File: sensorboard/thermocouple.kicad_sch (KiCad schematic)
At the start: 8 parts, among them U4 MAX31856

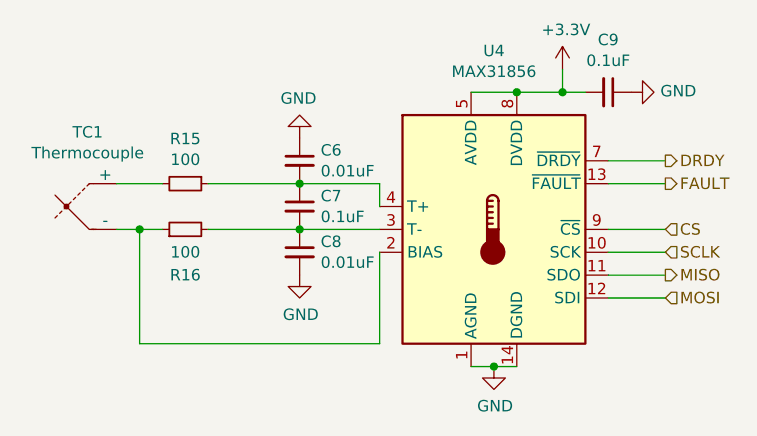
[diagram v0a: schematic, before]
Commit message: updated boost converter schematic, 5V lines
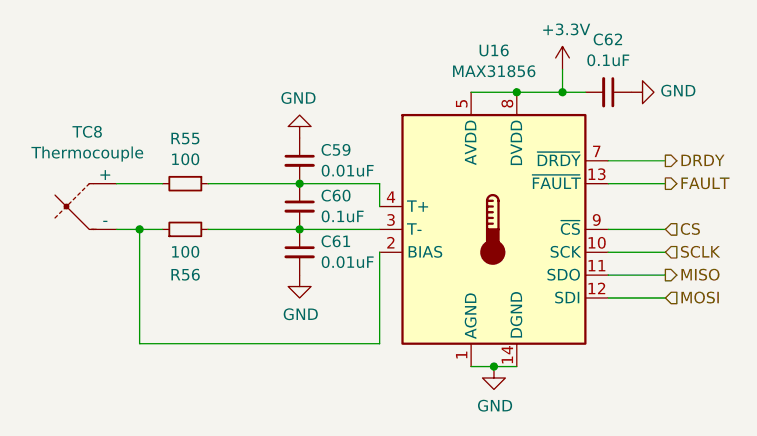
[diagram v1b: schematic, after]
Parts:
- renumbered C6 to C59, C7 to C60, C8 to C61, C9 to C62, R15 to R55, R16 to R56, TC1 to TC8, U4 to U16
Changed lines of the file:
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@@
   (symbol (lib_id "Sensor_Temperature:MAX31856") (at 95.25 73.66 0)
     (in_bom yes) (on_board yes)
-    (property "Reference" "U4" (id 0) (at 95.25 53.8226 0))
+    (property "Reference" "U16" (id 0) (at 95.25 53.8226 0))
     (property "Value" "MAX31856" (id 1) (at 95.25 56.134 0))
     (property "Footprint" "Package_SO:TSSOP-14_4.4x5mm_P0.65mm" (id 2) (at 99.06 87.63 0)
@@
   (symbol (lib_id "power:GND") (at 95.25 88.9 0)
     (in_bom yes) (on_board yes)
-    (property "Reference" "#PWR0130" (id 0) (at 95.25 95.25 0)
+    (property "Reference" "#PWR0120" (id 0) (at 95.25 95.25 0)
       (effects (font (size 1.27 1.27)) hide)
     )
@@
   (symbol (lib_id "analogue-cache:+3.3V") (at 102.87 55.88 0)
     (in_bom yes) (on_board yes)
-    (property "Reference" "#PWR0131" (id 0) (at 102.87 59.69 0)
+    (property "Reference" "#PWR0121" (id 0) (at 102.87 59.69 0)
       (effects (font (size 1.27 1.27)) hide)
     )
@@
   (symbol (lib_id "Device:C_Small") (at 107.95 58.42 270)
     (in_bom yes) (on_board yes)
-    (property "Reference" "C9" (id 0) (at 107.95 52.6034 90))
+    (property "Reference" "C62" (id 0) (at 107.95 52.6034 90))
     (property "Value" "0.1uF" (id 1) (at 107.95 54.9148 90))
     (property "Footprint" "Capacitor_SMD:C_0603_1608Metric" (id 2) (at 107.95 58.42 0)
@@
   (symbol (lib_id "power:GND") (at 110.49 58.42 90)
     (in_bom yes) (on_board yes)
-    (property "Reference" "#PWR0132" (id 0) (at 116.84 58.42 0)
+    (property "Reference" "#PWR0122" (id 0) (at 116.84 58.42 0)
       (effects (font (size 1.27 1.27)) hide)
     )
@@
   (symbol (lib_id "Device:Thermocouple") (at 50.8 71.12 0)
     (in_bom yes) (on_board yes)
-    (property "Reference" "TC1" (id 0) (at 50.1142 62.865 0))
+    (property "Reference" "TC8" (id 0) (at 50.1142 62.865 0))
     (property "Value" "Thermocouple" (id 1) (at 50.1142 65.1764 0))
     (property "Footprint" "TerminalBlock_TE-Connectivity:TerminalBlock_TE_282834-2_1x02_P2.54mm_Horizontal" (id 2) (at 36.195 69.85 0)
@@
   (symbol (lib_id "Device:R_Small") (at 60.96 68.58 270)
     (in_bom yes) (on_board yes)
-    (property "Reference" "R15" (id 0) (at 60.96 63.6016 90))
+    (property "Reference" "R55" (id 0) (at 60.96 63.6016 90))
     (property "Value" "100" (id 1) (at 60.96 65.913 90))
     (property "Footprint" "Resistor_SMD:R_0603_1608Metric" (id 2) (at 60.96 68.58 0)
@@
   (symbol (lib_id "Device:R_Small") (at 60.96 73.66 90)
     (in_bom yes) (on_board yes)
-    (property "Reference" "R16" (id 0) (at 60.96 78.74 90))
+    (property "Reference" "R56" (id 0) (at 60.96 78.74 90))
     (property "Value" "100" (id 1) (at 60.96 76.2 90))
     (property "Footprint" "Resistor_SMD:R_0603_1608Metric" (id 2) (at 60.96 73.66 0)
@@
   (symbol (lib_id "Device:C_Small") (at 73.66 71.12 0)
     (in_bom yes) (on_board yes)
-    (property "Reference" "C7" (id 0) (at 75.9968 69.9516 0)
+    (property "Reference" "C60" (id 0) (at 75.9968 69.9516 0)
       (effects (font (size 1.27 1.27)) (justify left))
     )
@@
   (symbol (lib_id "Device:C_Small") (at 73.66 66.04 0)
     (in_bom yes) (on_board yes)
-    (property "Reference" "C6" (id 0) (at 75.9968 64.8716 0)
+    (property "Reference" "C59" (id 0) (at 75.9968 64.8716 0)
       (effects (font (size 1.27 1.27)) (justify left))
     )
@@
   (symbol (lib_id "Device:C_Small") (at 73.66 76.2 0)
     (in_bom yes) (on_board yes)
-    (property "Reference" "C8" (id 0) (at 75.9968 75.0316 0)
+    (property "Reference" "C61" (id 0) (at 75.9968 75.0316 0)
       (effects (font (size 1.27 1.27)) (justify left))
     )
@@
   (symbol (lib_id "power:GND") (at 73.66 78.74 0)
     (in_bom yes) (on_board yes)
-    (property "Reference" "#PWR0129" (id 0) (at 73.66 85.09 0)
+    (property "Reference" "#PWR0119" (id 0) (at 73.66 85.09 0)
       (effects (font (size 1.27 1.27)) hide)
     )
@@
   (symbol (lib_id "power:GND") (at 73.66 63.5 180)
     (in_bom yes) (on_board yes)
-    (property "Reference" "#PWR0128" (id 0) (at 73.66 57.15 0)
+    (property "Reference" "#PWR0118" (id 0) (at 73.66 57.15 0)
       (effects (font (size 1.27 1.27)) hide)
     )

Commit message: LEDs and repositioning for 5V
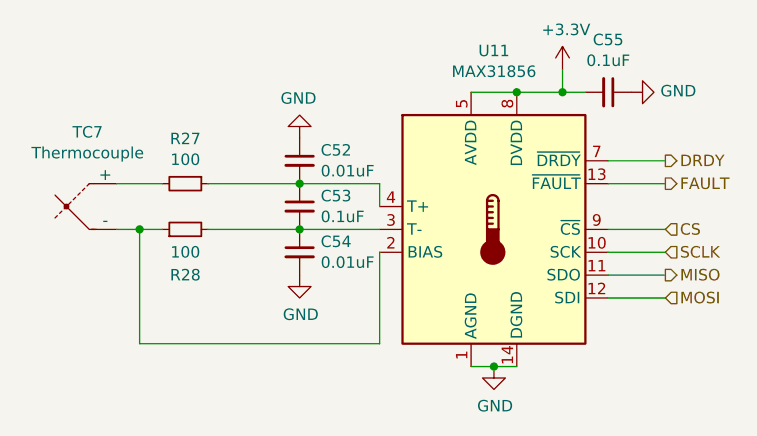
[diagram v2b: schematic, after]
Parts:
- renumbered C59 to C52, C60 to C53, C61 to C54, C62 to C55, R55 to R27, R56 to R28, TC8 to TC7, U16 to U11
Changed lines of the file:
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@@
   (symbol (lib_id "Sensor_Temperature:MAX31856") (at 95.25 73.66 0)
     (in_bom yes) (on_board yes)
-    (property "Reference" "U16" (id 0) (at 95.25 53.8226 0))
+    (property "Reference" "U11" (id 0) (at 95.25 53.8226 0))
     (property "Value" "MAX31856" (id 1) (at 95.25 56.134 0))
     (property "Footprint" "Package_SO:TSSOP-14_4.4x5mm_P0.65mm" (id 2) (at 99.06 87.63 0)
@@
   (symbol (lib_id "power:GND") (at 95.25 88.9 0)
     (in_bom yes) (on_board yes)
-    (property "Reference" "#PWR0120" (id 0) (at 95.25 95.25 0)
+    (property "Reference" "#PWR0130" (id 0) (at 95.25 95.25 0)
       (effects (font (size 1.27 1.27)) hide)
     )
@@
   (symbol (lib_id "analogue-cache:+3.3V") (at 102.87 55.88 0)
     (in_bom yes) (on_board yes)
-    (property "Reference" "#PWR0121" (id 0) (at 102.87 59.69 0)
+    (property "Reference" "#PWR0131" (id 0) (at 102.87 59.69 0)
       (effects (font (size 1.27 1.27)) hide)
     )
@@
   (symbol (lib_id "Device:C_Small") (at 107.95 58.42 270)
     (in_bom yes) (on_board yes)
-    (property "Reference" "C62" (id 0) (at 107.95 52.6034 90))
+    (property "Reference" "C55" (id 0) (at 107.95 52.6034 90))
     (property "Value" "0.1uF" (id 1) (at 107.95 54.9148 90))
     (property "Footprint" "Capacitor_SMD:C_0603_1608Metric" (id 2) (at 107.95 58.42 0)
@@
   (symbol (lib_id "power:GND") (at 110.49 58.42 90)
     (in_bom yes) (on_board yes)
-    (property "Reference" "#PWR0122" (id 0) (at 116.84 58.42 0)
+    (property "Reference" "#PWR0132" (id 0) (at 116.84 58.42 0)
       (effects (font (size 1.27 1.27)) hide)
     )
@@
   (symbol (lib_id "Device:Thermocouple") (at 50.8 71.12 0)
     (in_bom yes) (on_board yes)
-    (property "Reference" "TC8" (id 0) (at 50.1142 62.865 0))
+    (property "Reference" "TC7" (id 0) (at 50.1142 62.865 0))
     (property "Value" "Thermocouple" (id 1) (at 50.1142 65.1764 0))
     (property "Footprint" "TerminalBlock_TE-Connectivity:TerminalBlock_TE_282834-2_1x02_P2.54mm_Horizontal" (id 2) (at 36.195 69.85 0)
@@
   (symbol (lib_id "Device:R_Small") (at 60.96 68.58 270)
     (in_bom yes) (on_board yes)
-    (property "Reference" "R55" (id 0) (at 60.96 63.6016 90))
+    (property "Reference" "R27" (id 0) (at 60.96 63.6016 90))
     (property "Value" "100" (id 1) (at 60.96 65.913 90))
     (property "Footprint" "Resistor_SMD:R_0603_1608Metric" (id 2) (at 60.96 68.58 0)
@@
   (symbol (lib_id "Device:R_Small") (at 60.96 73.66 90)
     (in_bom yes) (on_board yes)
-    (property "Reference" "R56" (id 0) (at 60.96 78.74 90))
+    (property "Reference" "R28" (id 0) (at 60.96 78.74 90))
     (property "Value" "100" (id 1) (at 60.96 76.2 90))
     (property "Footprint" "Resistor_SMD:R_0603_1608Metric" (id 2) (at 60.96 73.66 0)
@@
   (symbol (lib_id "Device:C_Small") (at 73.66 71.12 0)
     (in_bom yes) (on_board yes)
-    (property "Reference" "C60" (id 0) (at 75.9968 69.9516 0)
+    (property "Reference" "C53" (id 0) (at 75.9968 69.9516 0)
       (effects (font (size 1.27 1.27)) (justify left))
     )
@@
   (symbol (lib_id "Device:C_Small") (at 73.66 66.04 0)
     (in_bom yes) (on_board yes)
-    (property "Reference" "C59" (id 0) (at 75.9968 64.8716 0)
+    (property "Reference" "C52" (id 0) (at 75.9968 64.8716 0)
       (effects (font (size 1.27 1.27)) (justify left))
     )
@@
   (symbol (lib_id "Device:C_Small") (at 73.66 76.2 0)
     (in_bom yes) (on_board yes)
-    (property "Reference" "C61" (id 0) (at 75.9968 75.0316 0)
+    (property "Reference" "C54" (id 0) (at 75.9968 75.0316 0)
       (effects (font (size 1.27 1.27)) (justify left))
     )
@@
   (symbol (lib_id "power:GND") (at 73.66 78.74 0)
     (in_bom yes) (on_board yes)
-    (property "Reference" "#PWR0119" (id 0) (at 73.66 85.09 0)
+    (property "Reference" "#PWR0129" (id 0) (at 73.66 85.09 0)
       (effects (font (size 1.27 1.27)) hide)
     )
@@
   (symbol (lib_id "power:GND") (at 73.66 63.5 180)
     (in_bom yes) (on_board yes)
-    (property "Reference" "#PWR0118" (id 0) (at 73.66 57.15 0)
+    (property "Reference" "#PWR0128" (id 0) (at 73.66 57.15 0)
       (effects (font (size 1.27 1.27)) hide)
     )

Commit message: Swapped the antenna for the coaxial connector
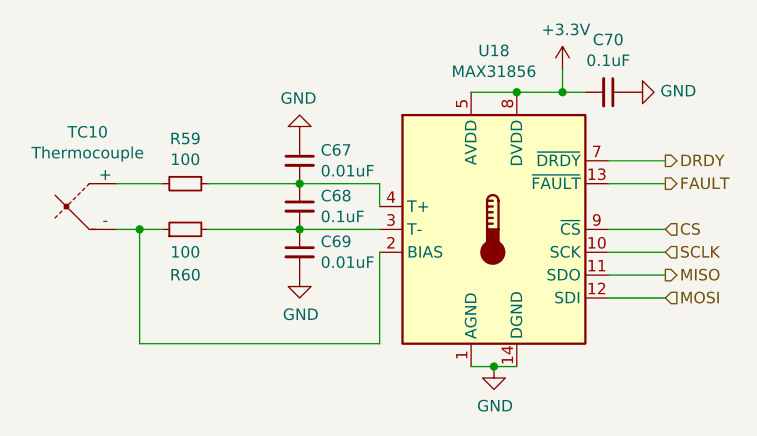
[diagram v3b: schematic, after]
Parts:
- renumbered C52 to C67, C53 to C68, C54 to C69, C55 to C70, R27 to R59, R28 to R60, TC7 to TC10, U11 to U18
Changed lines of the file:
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@@
   (symbol (lib_id "Sensor_Temperature:MAX31856") (at 95.25 73.66 0)
     (in_bom yes) (on_board yes)
-    (property "Reference" "U11" (id 0) (at 95.25 53.8226 0))
+    (property "Reference" "U18" (id 0) (at 95.25 53.8226 0))
     (property "Value" "MAX31856" (id 1) (at 95.25 56.134 0))
     (property "Footprint" "Package_SO:TSSOP-14_4.4x5mm_P0.65mm" (id 2) (at 99.06 87.63 0)
@@
   (symbol (lib_id "Device:C_Small") (at 107.95 58.42 270)
     (in_bom yes) (on_board yes)
-    (property "Reference" "C55" (id 0) (at 107.95 52.6034 90))
+    (property "Reference" "C70" (id 0) (at 107.95 52.6034 90))
     (property "Value" "0.1uF" (id 1) (at 107.95 54.9148 90))
     (property "Footprint" "Capacitor_SMD:C_0603_1608Metric" (id 2) (at 107.95 58.42 0)
@@
   (symbol (lib_id "Device:Thermocouple") (at 50.8 71.12 0)
     (in_bom yes) (on_board yes)
-    (property "Reference" "TC7" (id 0) (at 50.1142 62.865 0))
+    (property "Reference" "TC10" (id 0) (at 50.1142 62.865 0))
     (property "Value" "Thermocouple" (id 1) (at 50.1142 65.1764 0))
     (property "Footprint" "TerminalBlock_TE-Connectivity:TerminalBlock_TE_282834-2_1x02_P2.54mm_Horizontal" (id 2) (at 36.195 69.85 0)
@@
   (symbol (lib_id "Device:R_Small") (at 60.96 68.58 270)
     (in_bom yes) (on_board yes)
-    (property "Reference" "R27" (id 0) (at 60.96 63.6016 90))
+    (property "Reference" "R59" (id 0) (at 60.96 63.6016 90))
     (property "Value" "100" (id 1) (at 60.96 65.913 90))
     (property "Footprint" "Resistor_SMD:R_0603_1608Metric" (id 2) (at 60.96 68.58 0)
@@
   (symbol (lib_id "Device:R_Small") (at 60.96 73.66 90)
     (in_bom yes) (on_board yes)
-    (property "Reference" "R28" (id 0) (at 60.96 78.74 90))
+    (property "Reference" "R60" (id 0) (at 60.96 78.74 90))
     (property "Value" "100" (id 1) (at 60.96 76.2 90))
     (property "Footprint" "Resistor_SMD:R_0603_1608Metric" (id 2) (at 60.96 73.66 0)
@@
   (symbol (lib_id "Device:C_Small") (at 73.66 71.12 0)
     (in_bom yes) (on_board yes)
-    (property "Reference" "C53" (id 0) (at 75.9968 69.9516 0)
+    (property "Reference" "C68" (id 0) (at 75.9968 69.9516 0)
       (effects (font (size 1.27 1.27)) (justify left))
     )
@@
   (symbol (lib_id "Device:C_Small") (at 73.66 66.04 0)
     (in_bom yes) (on_board yes)
-    (property "Reference" "C52" (id 0) (at 75.9968 64.8716 0)
+    (property "Reference" "C67" (id 0) (at 75.9968 64.8716 0)
       (effects (font (size 1.27 1.27)) (justify left))
     )
@@
   (symbol (lib_id "Device:C_Small") (at 73.66 76.2 0)
     (in_bom yes) (on_board yes)
-    (property "Reference" "C54" (id 0) (at 75.9968 75.0316 0)
+    (property "Reference" "C69" (id 0) (at 75.9968 75.0316 0)
       (effects (font (size 1.27 1.27)) (justify left))
     )

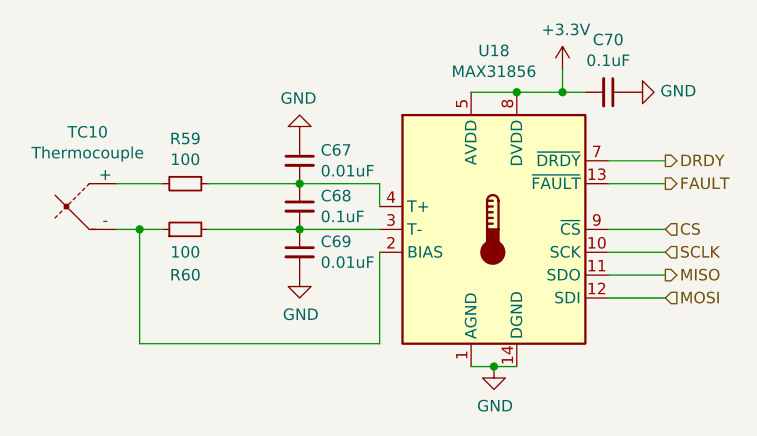
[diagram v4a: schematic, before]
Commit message: antenna and thermocouple prelim
Preliminary layout for thermocouples and antenna structure done
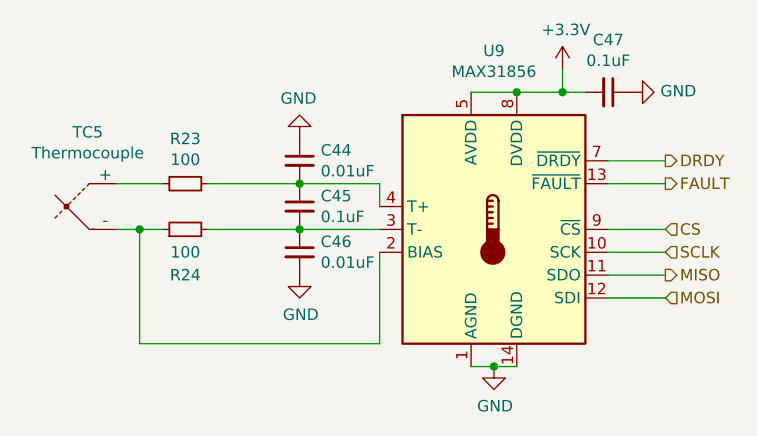
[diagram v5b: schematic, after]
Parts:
- renumbered C67 to C44, C68 to C45, C69 to C46, C70 to C47, R59 to R23, R60 to R24, TC10 to TC5, U18 to U9
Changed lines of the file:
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@@
   (symbol (lib_id "Sensor_Temperature:MAX31856") (at 95.25 73.66 0)
     (in_bom yes) (on_board yes)
-    (property "Reference" "U18" (id 0) (at 95.25 53.8226 0))
+    (property "Reference" "U9" (id 0) (at 95.25 53.8226 0))
     (property "Value" "MAX31856" (id 1) (at 95.25 56.134 0))
     (property "Footprint" "Package_SO:TSSOP-14_4.4x5mm_P0.65mm" (id 2) (at 99.06 87.63 0)
@@
   (symbol (lib_id "Device:C_Small") (at 107.95 58.42 270)
     (in_bom yes) (on_board yes)
-    (property "Reference" "C70" (id 0) (at 107.95 52.6034 90))
+    (property "Reference" "C47" (id 0) (at 107.95 52.6034 90))
     (property "Value" "0.1uF" (id 1) (at 107.95 54.9148 90))
     (property "Footprint" "Capacitor_SMD:C_0603_1608Metric" (id 2) (at 107.95 58.42 0)
@@
   (symbol (lib_id "Device:Thermocouple") (at 50.8 71.12 0)
     (in_bom yes) (on_board yes)
-    (property "Reference" "TC10" (id 0) (at 50.1142 62.865 0))
+    (property "Reference" "TC5" (id 0) (at 50.1142 62.865 0))
     (property "Value" "Thermocouple" (id 1) (at 50.1142 65.1764 0))
     (property "Footprint" "TerminalBlock_TE-Connectivity:TerminalBlock_TE_282834-2_1x02_P2.54mm_Horizontal" (id 2) (at 36.195 69.85 0)
@@
   (symbol (lib_id "Device:R_Small") (at 60.96 68.58 270)
     (in_bom yes) (on_board yes)
-    (property "Reference" "R59" (id 0) (at 60.96 63.6016 90))
+    (property "Reference" "R23" (id 0) (at 60.96 63.6016 90))
     (property "Value" "100" (id 1) (at 60.96 65.913 90))
     (property "Footprint" "Resistor_SMD:R_0603_1608Metric" (id 2) (at 60.96 68.58 0)
@@
   (symbol (lib_id "Device:R_Small") (at 60.96 73.66 90)
     (in_bom yes) (on_board yes)
-    (property "Reference" "R60" (id 0) (at 60.96 78.74 90))
+    (property "Reference" "R24" (id 0) (at 60.96 78.74 90))
     (property "Value" "100" (id 1) (at 60.96 76.2 90))
     (property "Footprint" "Resistor_SMD:R_0603_1608Metric" (id 2) (at 60.96 73.66 0)
@@
   (symbol (lib_id "Device:C_Small") (at 73.66 71.12 0)
     (in_bom yes) (on_board yes)
-    (property "Reference" "C68" (id 0) (at 75.9968 69.9516 0)
+    (property "Reference" "C45" (id 0) (at 75.9968 69.9516 0)
       (effects (font (size 1.27 1.27)) (justify left))
     )
@@
   (symbol (lib_id "Device:C_Small") (at 73.66 66.04 0)
     (in_bom yes) (on_board yes)
-    (property "Reference" "C67" (id 0) (at 75.9968 64.8716 0)
+    (property "Reference" "C44" (id 0) (at 75.9968 64.8716 0)
       (effects (font (size 1.27 1.27)) (justify left))
     )
@@
   (symbol (lib_id "Device:C_Small") (at 73.66 76.2 0)
     (in_bom yes) (on_board yes)
-    (property "Reference" "C69" (id 0) (at 75.9968 75.0316 0)
+    (property "Reference" "C46" (id 0) (at 75.9968 75.0316 0)
       (effects (font (size 1.27 1.27)) (justify left))
     )

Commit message: Changed diode fps from castellated
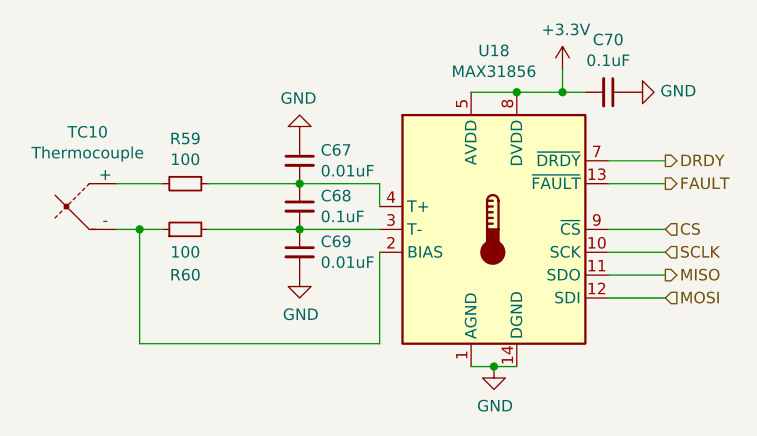
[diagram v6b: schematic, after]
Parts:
- renumbered C44 to C67, C45 to C68, C46 to C69, C47 to C70, R23 to R59, R24 to R60, TC5 to TC10, U9 to U18
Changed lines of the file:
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@@
   (symbol (lib_id "Sensor_Temperature:MAX31856") (at 95.25 73.66 0)
     (in_bom yes) (on_board yes)
-    (property "Reference" "U9" (id 0) (at 95.25 53.8226 0))
+    (property "Reference" "U18" (id 0) (at 95.25 53.8226 0))
     (property "Value" "MAX31856" (id 1) (at 95.25 56.134 0))
     (property "Footprint" "Package_SO:TSSOP-14_4.4x5mm_P0.65mm" (id 2) (at 99.06 87.63 0)
@@
   (symbol (lib_id "Device:C_Small") (at 107.95 58.42 270)
     (in_bom yes) (on_board yes)
-    (property "Reference" "C47" (id 0) (at 107.95 52.6034 90))
+    (property "Reference" "C70" (id 0) (at 107.95 52.6034 90))
     (property "Value" "0.1uF" (id 1) (at 107.95 54.9148 90))
     (property "Footprint" "Capacitor_SMD:C_0603_1608Metric" (id 2) (at 107.95 58.42 0)
@@
   (symbol (lib_id "Device:Thermocouple") (at 50.8 71.12 0)
     (in_bom yes) (on_board yes)
-    (property "Reference" "TC5" (id 0) (at 50.1142 62.865 0))
+    (property "Reference" "TC10" (id 0) (at 50.1142 62.865 0))
     (property "Value" "Thermocouple" (id 1) (at 50.1142 65.1764 0))
     (property "Footprint" "TerminalBlock_TE-Connectivity:TerminalBlock_TE_282834-2_1x02_P2.54mm_Horizontal" (id 2) (at 36.195 69.85 0)
@@
   (symbol (lib_id "Device:R_Small") (at 60.96 68.58 270)
     (in_bom yes) (on_board yes)
-    (property "Reference" "R23" (id 0) (at 60.96 63.6016 90))
+    (property "Reference" "R59" (id 0) (at 60.96 63.6016 90))
     (property "Value" "100" (id 1) (at 60.96 65.913 90))
     (property "Footprint" "Resistor_SMD:R_0603_1608Metric" (id 2) (at 60.96 68.58 0)
@@
   (symbol (lib_id "Device:R_Small") (at 60.96 73.66 90)
     (in_bom yes) (on_board yes)
-    (property "Reference" "R24" (id 0) (at 60.96 78.74 90))
+    (property "Reference" "R60" (id 0) (at 60.96 78.74 90))
     (property "Value" "100" (id 1) (at 60.96 76.2 90))
     (property "Footprint" "Resistor_SMD:R_0603_1608Metric" (id 2) (at 60.96 73.66 0)
@@
   (symbol (lib_id "Device:C_Small") (at 73.66 71.12 0)
     (in_bom yes) (on_board yes)
-    (property "Reference" "C45" (id 0) (at 75.9968 69.9516 0)
+    (property "Reference" "C68" (id 0) (at 75.9968 69.9516 0)
       (effects (font (size 1.27 1.27)) (justify left))
     )
@@
   (symbol (lib_id "Device:C_Small") (at 73.66 66.04 0)
     (in_bom yes) (on_board yes)
-    (property "Reference" "C44" (id 0) (at 75.9968 64.8716 0)
+    (property "Reference" "C67" (id 0) (at 75.9968 64.8716 0)
       (effects (font (size 1.27 1.27)) (justify left))
     )
@@
   (symbol (lib_id "Device:C_Small") (at 73.66 76.2 0)
     (in_bom yes) (on_board yes)
-    (property "Reference" "C46" (id 0) (at 75.9968 75.0316 0)
+    (property "Reference" "C69" (id 0) (at 75.9968 75.0316 0)
       (effects (font (size 1.27 1.27)) (justify left))
     )
